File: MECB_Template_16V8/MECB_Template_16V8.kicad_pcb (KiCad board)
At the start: 2 copper layers, 99.8 x 99.8 mm, 6 parts, among them J1 MECB_64AC, U1 ATF16V8

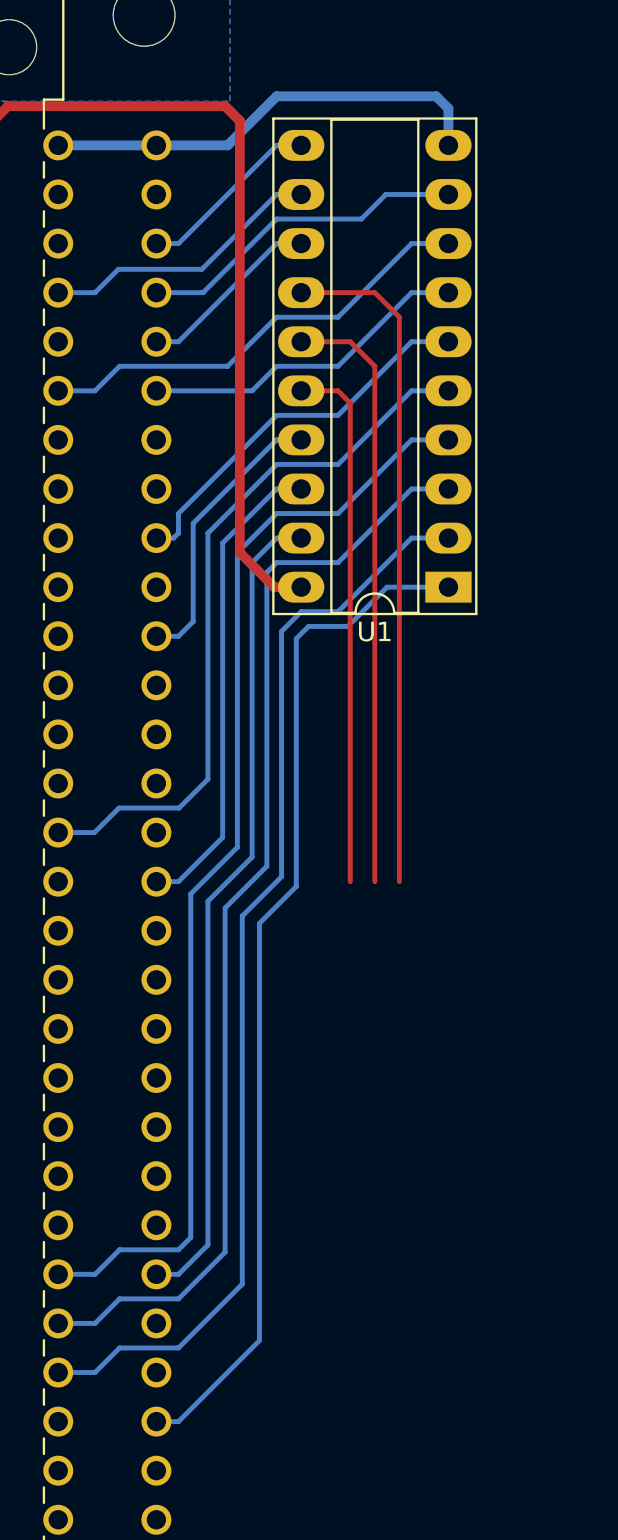
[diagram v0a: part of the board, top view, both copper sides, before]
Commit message: Update MECB KiCAD Templates. Include 220nf bypass capacitor. Re-route tracks based on new capacitor positioning. Update 3D images to be new blue colouring. Correct earth zone inner corner rounding.
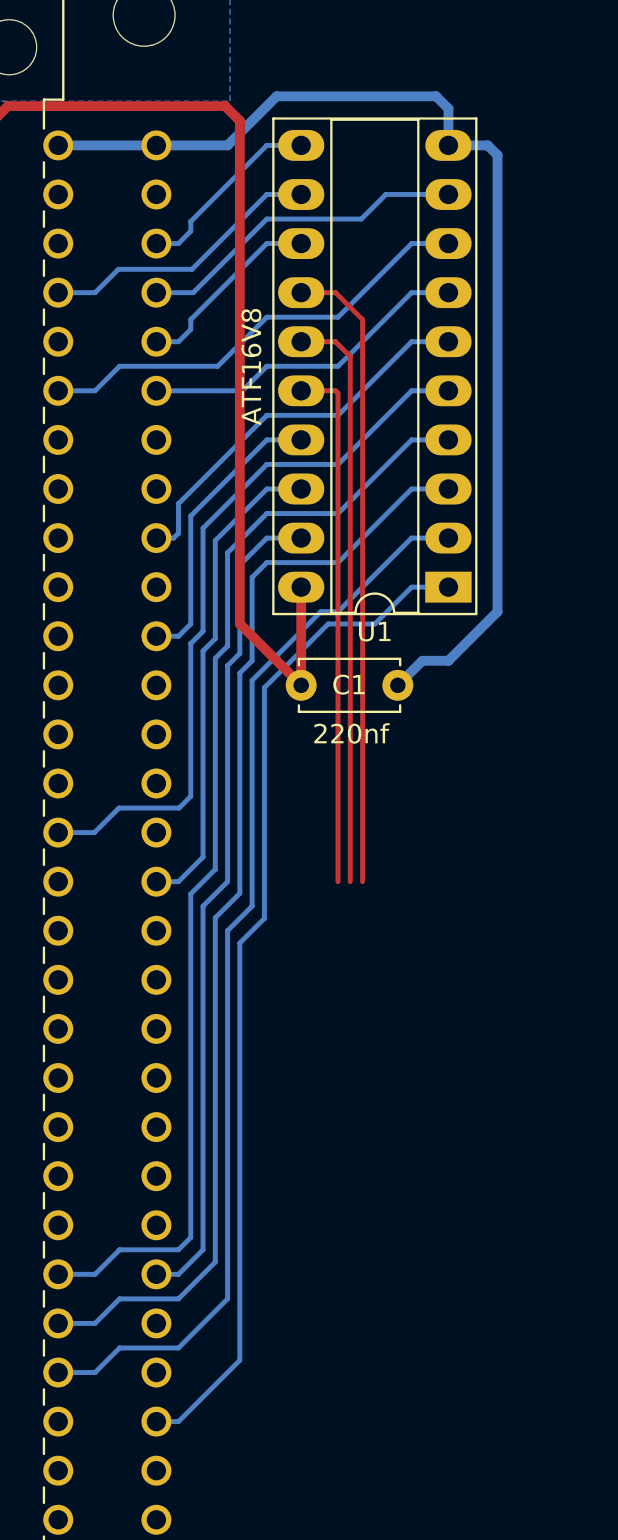
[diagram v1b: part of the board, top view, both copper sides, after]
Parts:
- added C1: 0.22uf, Capacitor_THT:C_Disc_D5.0mm_W2.5mm_P5.00mm, F.Cu at (114.3, 85.1)
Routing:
- net GND: track 23.4 -> 56.5 mm
- net +5V: track 127.7 -> 137.0 mm
- net CS0: track 34.8 -> 32.8 mm
- net CS1: track 31.0 -> 30.0 mm
- net /ECB_A4: track 56.7 -> 56.1 mm
- net /ECB_A3: track 53.2 -> 52.6 mm
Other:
- board text added: "220nf"
- board text added: "ATF16V8"
